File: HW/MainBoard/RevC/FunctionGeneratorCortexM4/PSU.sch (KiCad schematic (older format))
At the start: 37 parts, among them Q1 DMG2301L, U1 NCP51460SN33T1G, U3 LP3992-33B5F, U4 TRN 1-0522, U6 STM32G474RET, U8 LM1117-5.0

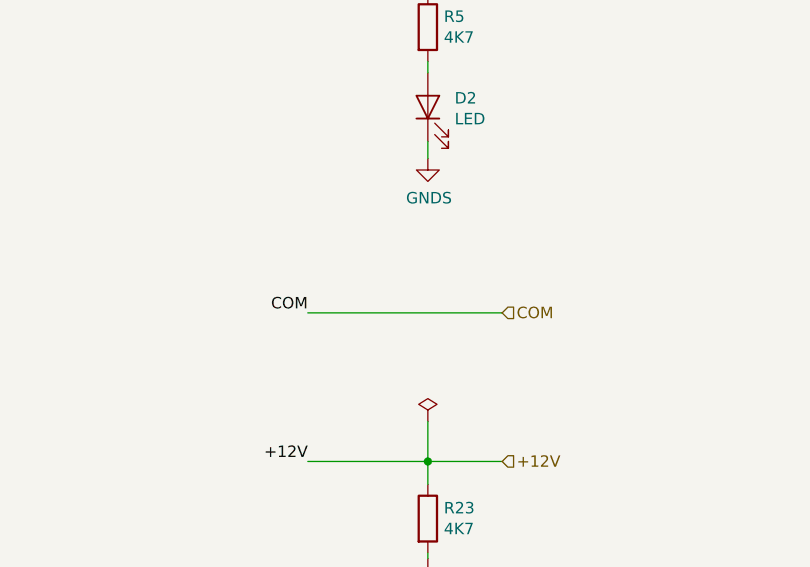
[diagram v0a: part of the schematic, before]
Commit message: Updated MainBoard RevC
- Block diagram and connections completed on schematic
- Need to check MCU pin availability
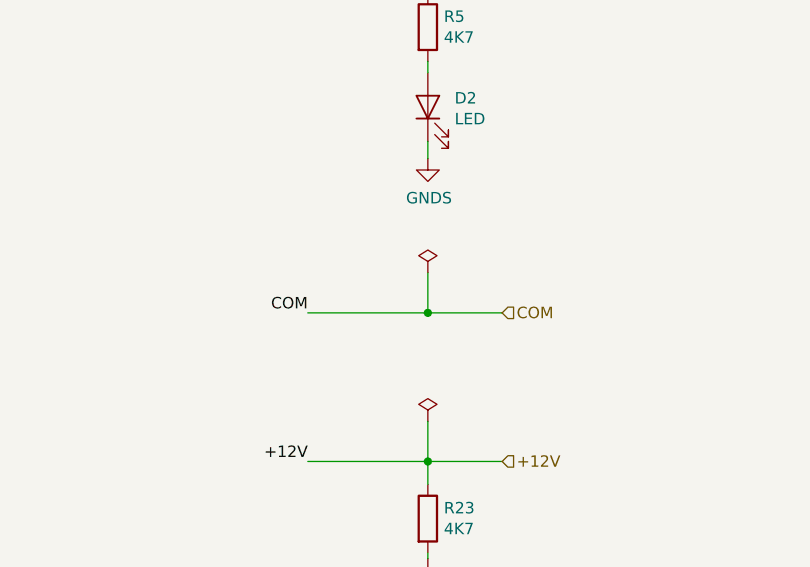
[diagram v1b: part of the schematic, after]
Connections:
- wire segments 141 -> 143
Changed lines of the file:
@@
 $Descr A3 16535 11693
 encoding utf-8
-Sheet 4 4
+Sheet 4 5
 Title "Power Supply"
 Date "2020-03-04"
@@
 +12V
 Wire Wire Line
-	13825 6075 14675 6075
+	13825 6075 14350 6075
 Text Label 13825 6075 2    50   ~ 0
 COM
@@
 Wire Wire Line
 	4650 4450 5725 4450
+$Comp
+L power:PWR_FLAG #FLG0102
+U 1 1 5F988E4B
+P 14350 5900
+F 0 "#FLG0102" H 14350 5975 50  0001 C CNN
+F 1 "PWR_FLAG" H 14350 6073 50  0001 C CNN
+F 2 "" H 14350 5900 50  0001 C CNN
+F 3 "~" H 14350 5900 50  0001 C CNN
+	1    14350 5900
+	1    0    0    -1
+$EndComp
+Wire Wire Line
+	14350 5900 14350 6075
+Connection ~ 14350 6075
+Wire Wire Line
+	14350 6075 14675 6075
 $EndSCHEMATC

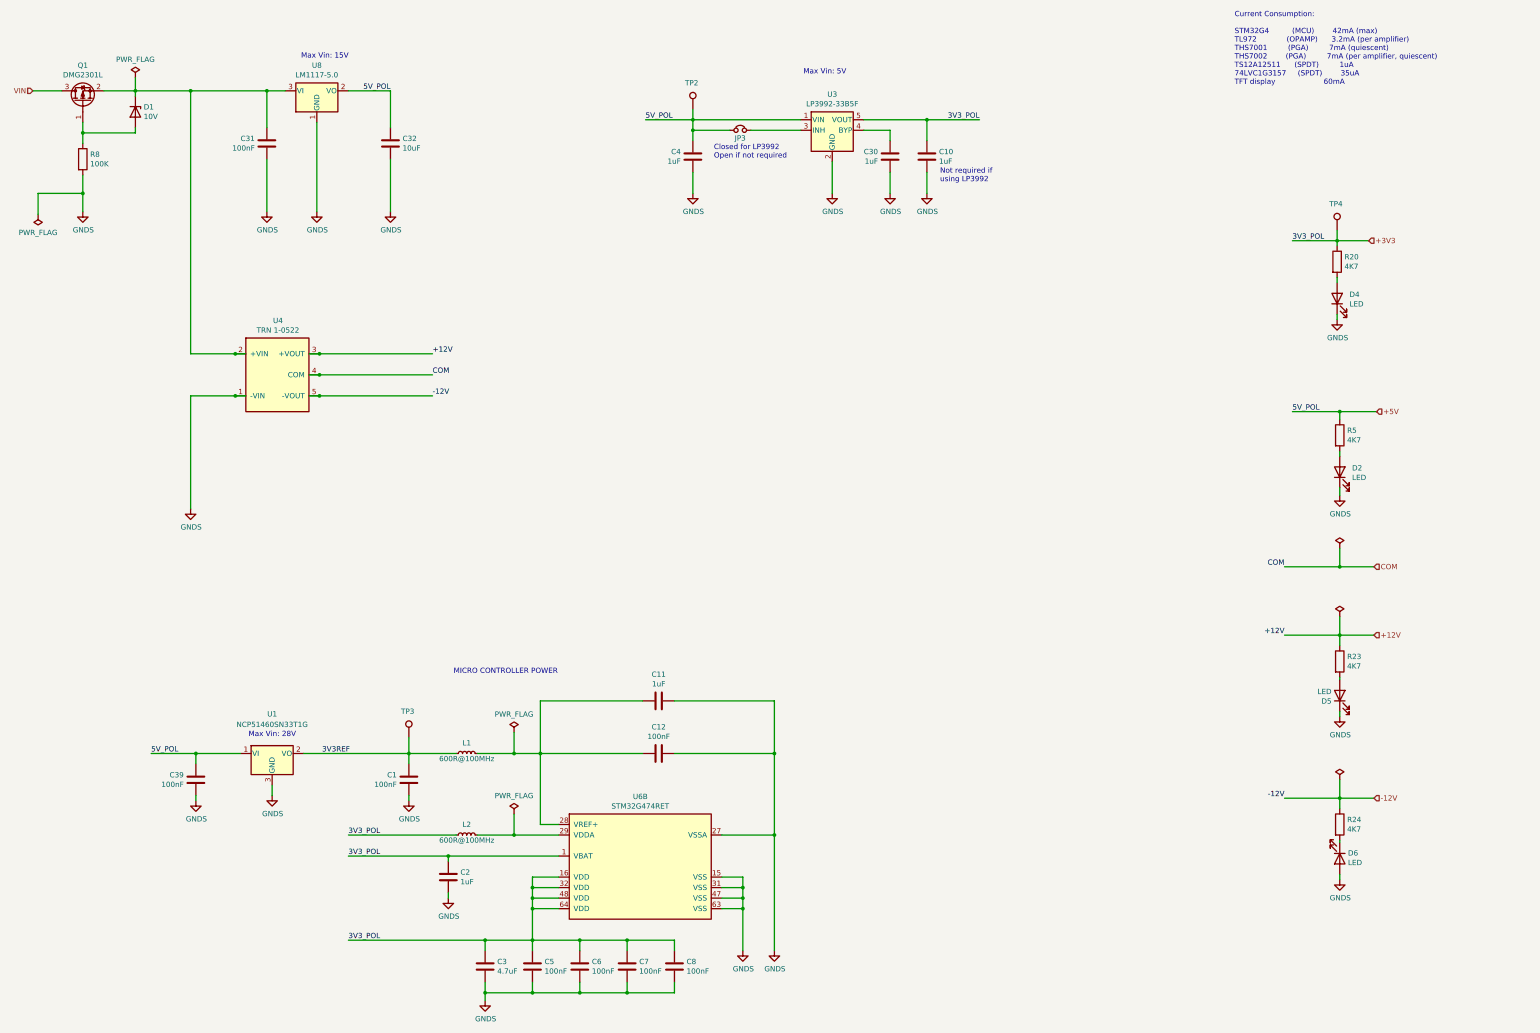
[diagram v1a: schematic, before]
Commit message: Added two-series resistors in PGA feedback
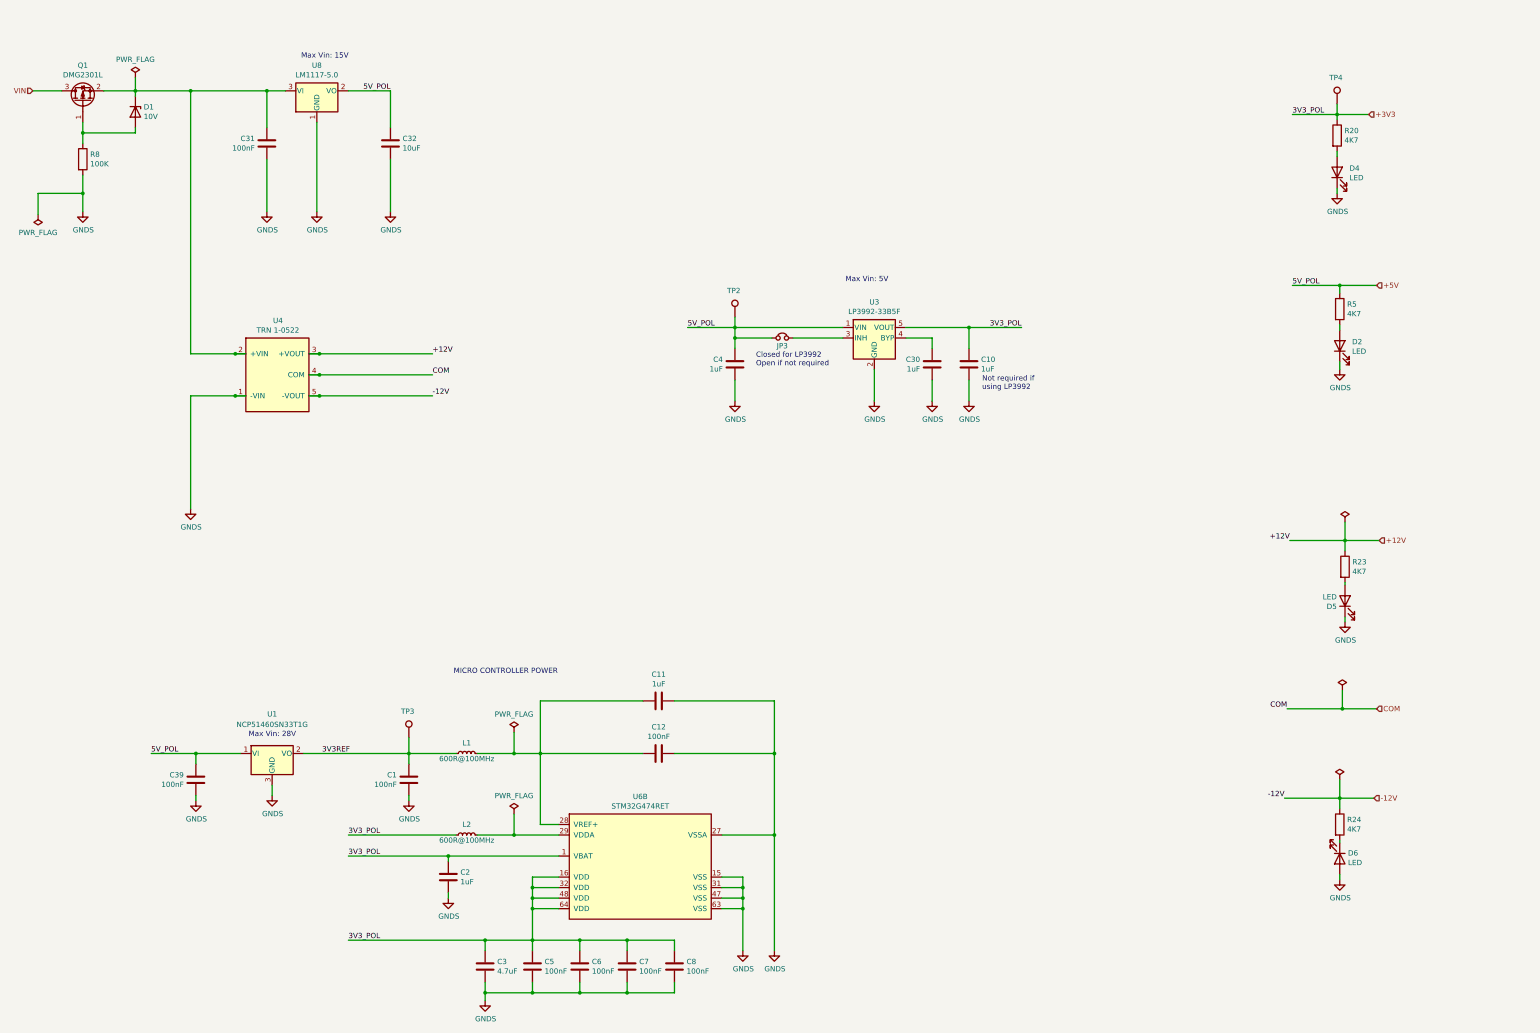
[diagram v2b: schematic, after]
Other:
- note removed: "Current Consumption:\n\nSTM32G4 (MCU) 42mA (max)\nTL972 (OPAMP) 3.2mA (per amplifier)\nTHS7001 (PGA) 7mA (quiescent)\nTHS7002 (PGA) 7mA (per amplifier, quiescent)\nTS12A12511 (SPDT) 1uA\n74LVC1G3157 (SPDT) 35uA\nTFT display 60mA"
- moved on the sheet: C10, C30, C4, D2, D4, D5, JP3, R20, R23, R5, TP2, TP4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
